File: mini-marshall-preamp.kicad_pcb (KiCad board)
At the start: 2 copper layers, 134 x 76.5 mm, 50 parts, among them J1 LO, J2 HI, J3 OUT, J4 6V3, J5 370V GND, J6 370V, J7 6V3 GND, J8 6V3, J9 6V3 GND, U1 6N2P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

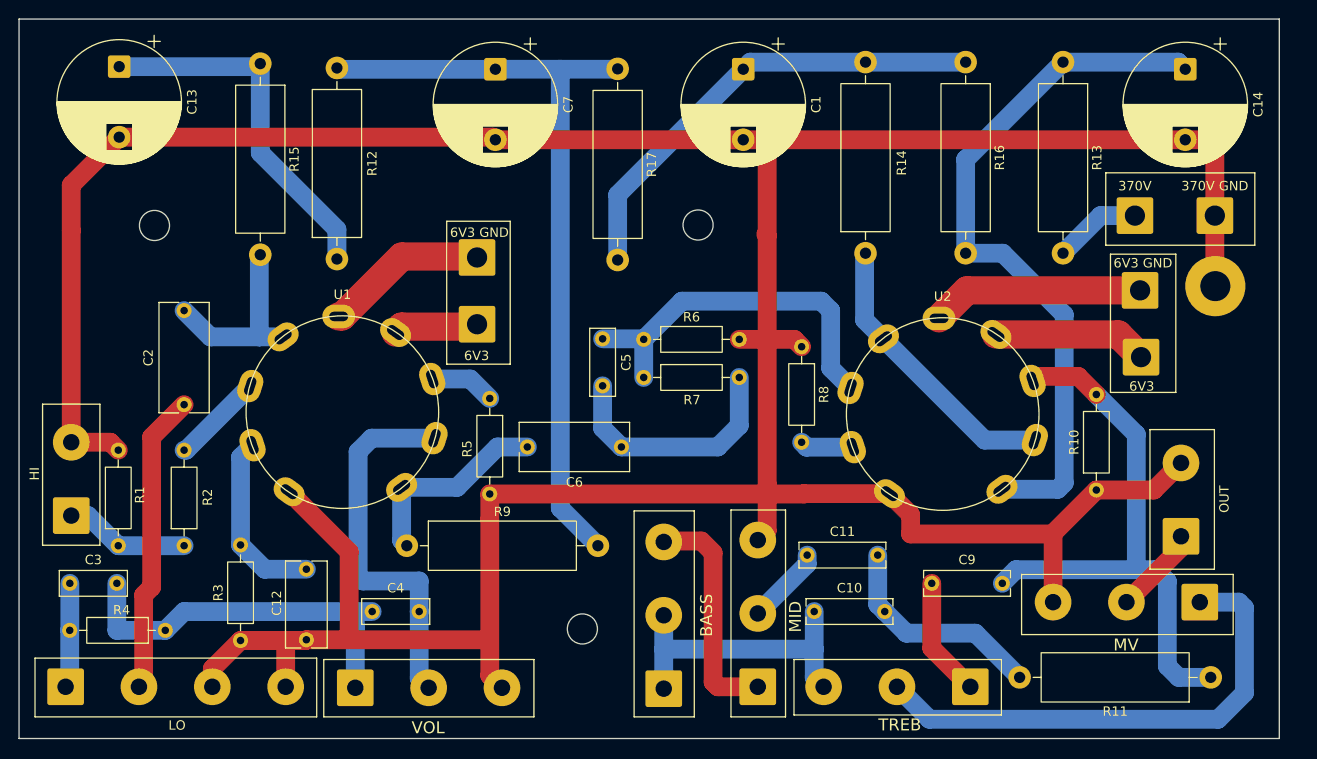
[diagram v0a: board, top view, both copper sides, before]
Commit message: Tune clearances
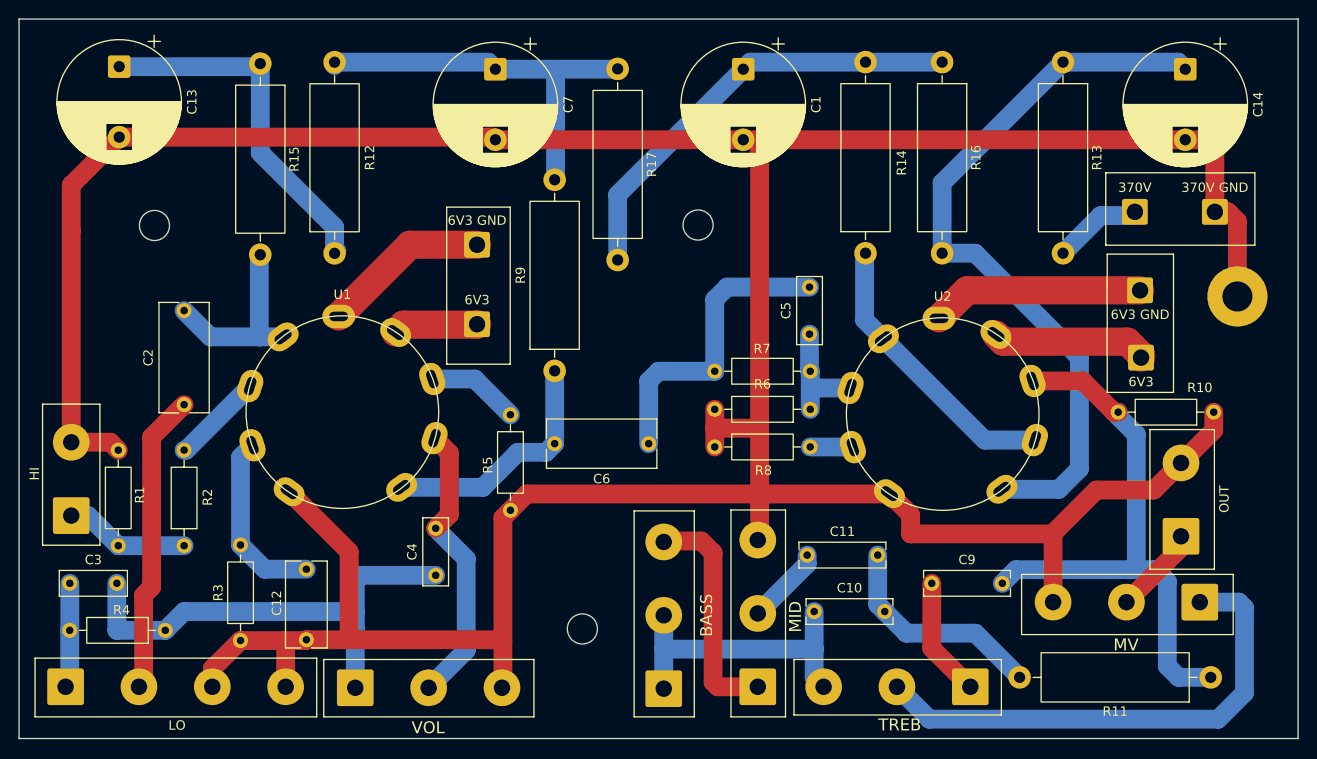
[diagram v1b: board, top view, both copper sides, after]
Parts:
- J4, J5, J6, J7, J8, J9: footprint Connector_Wire:SolderWire-1.5sqmm_1x01_D1.7mm_OD3.9mm -> Connector_Wire:SolderWire-1sqmm_1x01_D1.4mm_OD2.7mm
- moved R9 24.3 mm to (109.4, 87.4), turned to 90 degrees
- moved C5 22.0 mm to (136.5, 83.5), turned to 90 degrees
- moved R6 19.2 mm to (136.6, 91.5), turned to 180 degrees
- moved R7 17.7 mm to (136.6, 87.5), turned to 180 degrees
- moved R10 15.0 mm to (179.5, 91.8), turned to 180 degrees
- moved R8 14.1 mm to (126.4, 95.5), turned to 0 degrees
- moved C4 7.77 mm to (96.8, 109.2), turned to 90 degrees
- moved C6 2.92 mm to (119.4, 95.2)
- moved R5 2.80 mm to (104.7, 92.1)
- moved H3 2.59 mm to (182.0, 79.5)
- moved R16 2.50 mm to (150.6, 54.6)
- moved J9 1.35 mm to (101.2, 74.0)
- moved R12 0.66 mm to (86.0, 74.9)
- moved J5 0.40 mm to (179.6, 70.5)
- moved J6 0.40 mm to (171.1, 70.5)
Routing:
- net Net-(C7-Pad1): track 82.3 -> 42.6 mm
- net Net-(U2A-G): track 39.5 -> 12.3 mm
- net Net-(C3-Pad2): track 41.1 -> 51.3 mm
- net Net-(U1B-G): track 40.5 -> 30.8 mm
- net GND: track 386.8 -> 394.3 mm
- net Net-(C5-Pad2): track 25.9 -> 32.4 mm
- net Net-(U1B-A): track 21.6 -> 25.9 mm
- net /anode: track 75.9 -> 79.1 mm
- net Net-(U1B-K): track 6.97 -> 9.89 mm
- net Net-(C1-Pad1): track 49.8 -> 47.3 mm
- net Net-(U2A-K): track 5.66 -> 4.53 mm
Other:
- board size 134 x 76.5 mm -> 136 x 76.5 mm

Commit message: Track widths and prettifying
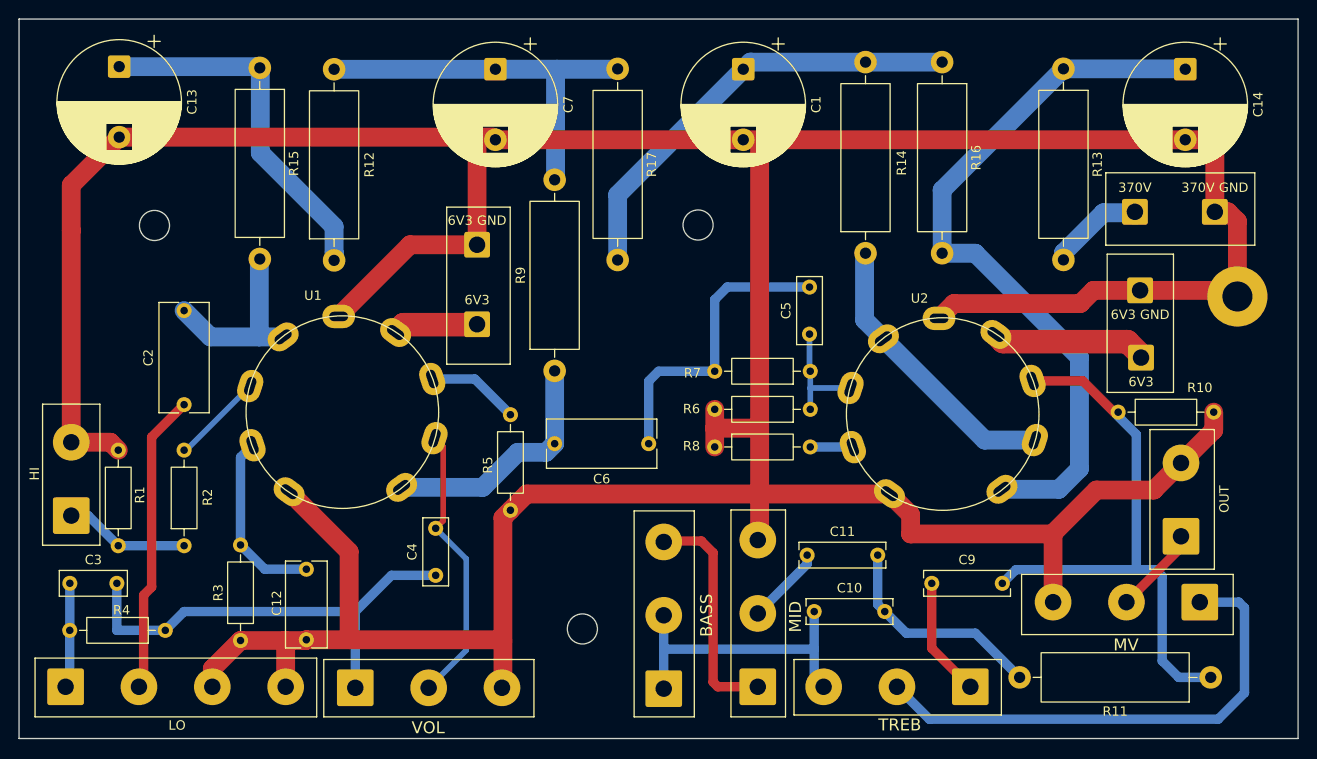
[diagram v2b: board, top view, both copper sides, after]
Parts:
- moved R12 0.75 mm to (86.0, 75.7)
- moved R13 0.71 mm to (163.5, 55.3)
- moved R15 0.45 mm to (78.0, 55.2)
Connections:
- net Net-(J4-Pin_1) renamed /U2-heater
- net Net-(J8-Pin_1) renamed /U1-heater
- J7 pad 1: GND1 -> GND
- J9 pad 1: GND1 -> GND
- U1 pad 5: GND1 -> GND
- U2 pad 5: GND1 -> GND
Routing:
- net GND: track 394.3 -> 456.9 mm
- net GND1: track 40.5 -> 0.00 mm
- net Net-(C3-Pad2): track 51.3 -> 49.4 mm
- net Net-(C13-Pad1): track 38.9 -> 37.9 mm
- net Net-(J6-Pin_1): track 9.30 -> 10.2 mm
- net /anode: track 79.1 -> 78.5 mm
- net Net-(C7-Pad1): track 42.6 -> 42.0 mm
- net Net-(U1B-G): track 30.8 -> 30.3 mm
